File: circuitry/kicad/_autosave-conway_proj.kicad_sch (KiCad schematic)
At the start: 5 parts, among them J1 Power, J2 Digital/PWM, J3 Analog, J4 Digital/PWM

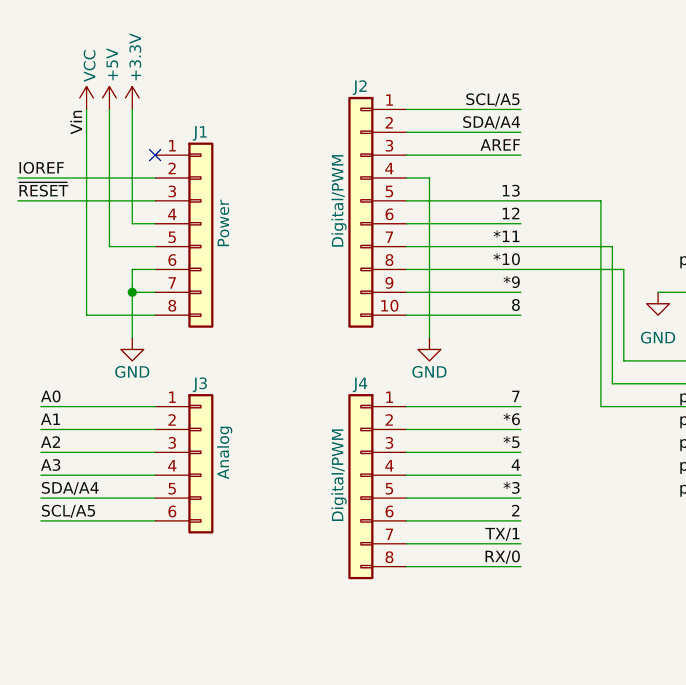
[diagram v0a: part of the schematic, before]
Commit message: New KiCad version and README updates
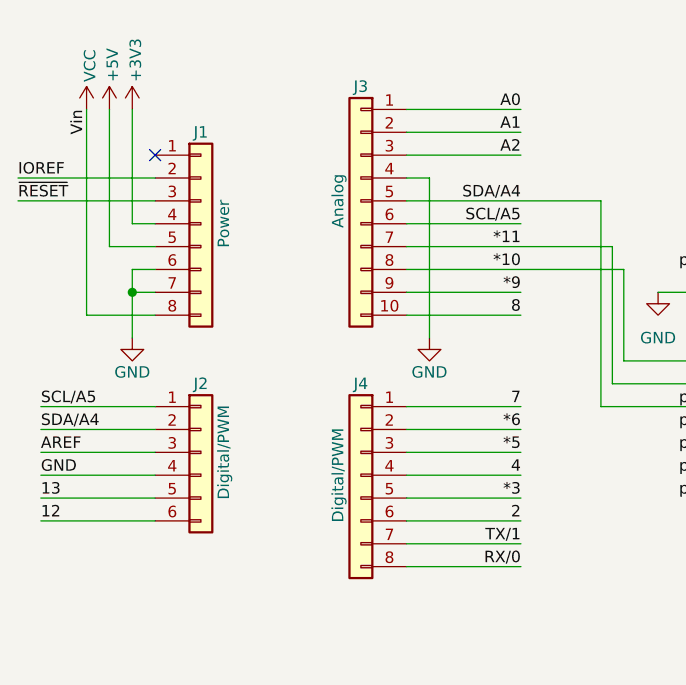
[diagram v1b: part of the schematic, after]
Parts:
- J2: renamed from J3; value Analog -> Digital/PWM; footprint Connector_PinSocket_2.54mm:PinSocket_1x06_P2.54mm_Vertical -> Connector_PinSocket_2.54mm:PinSocket_1x10_P2.54mm_Vertical
- J3: renamed from J2; value Digital/PWM -> Analog; footprint Connector_PinSocket_2.54mm:PinSocket_1x10_P2.54mm_Vertical -> Connector_PinSocket_2.54mm:PinSocket_1x06_P2.54mm_Vertical
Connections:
- net A3 is gone; now on net GND: J2.4 (Pin_4)
- net 12: now also J2.6 (Pin_6); no longer J3.6 (Pin_6)
- net 13: now also J2.5 (Pin_5); no longer DS1.6 (DB2), J3.5 (Pin_5)
- net A0: now also J3.1 (Pin_1); no longer J2.1 (Pin_1)
- net A1: now also J3.2 (Pin_2); no longer J2.2 (Pin_2)
- net A2: now also J3.3 (Pin_3); no longer J2.3 (Pin_3)
- net AREF: now also J2.3 (Pin_3); no longer J3.3 (Pin_3)
- net SCL/A5: now also J2.1 (Pin_1), J3.6 (Pin_6); no longer J2.6 (Pin_6), J3.1 (Pin_1)
- net SDA/A4: now also DS1.6 (DB2), J2.2 (Pin_2), J3.5 (Pin_5); no longer J2.5 (Pin_5), J3.2 (Pin_2)
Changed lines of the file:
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@@
     (effects (font (size 1.27 1.27)) (justify right bottom))
   )
-  (label "A2" (at 21.59 64.77 0) (fields_autoplaced)
+  (label "AREF" (at 21.59 64.77 0) (fields_autoplaced)
     (effects (font (size 1.27 1.27)) (justify left bottom))
   )
@@
     (effects (font (size 1.27 1.27)) (justify right bottom))
   )
-  (label "A3" (at 21.59 67.31 0) (fields_autoplaced)
+  (label "GND" (at 21.59 67.31 0) (fields_autoplaced)
     (effects (font (size 1.27 1.27)) (justify left bottom))
   )
@@
     (effects (font (size 1.27 1.27)) (justify right bottom))
   )
-  (label "13" (at 74.93 36.83 180) (fields_autoplaced)
-    (effects (font (size 1.27 1.27)) (justify right bottom))
-  )
-  (label "12" (at 74.93 39.37 180) (fields_autoplaced)
+  (label "SDA{slash}A4" (at 74.93 36.83 180) (fields_autoplaced)
+    (effects (font (size 1.27 1.27)) (justify right bottom))
+  )
+  (label "SCL{slash}A5" (at 74.93 39.37 180) (fields_autoplaced)
     (effects (font (size 1.27 1.27)) (justify right bottom))
   )
@@
     (effects (font (size 1.27 1.27)) (justify right bottom))
   )
-  (label "SDA{slash}A4" (at 74.93 29.21 180) (fields_autoplaced)
+  (label "A1" (at 74.93 29.21 180) (fields_autoplaced)
     (effects (font (size 1.27 1.27)) (justify right bottom))
   )
@@
     (effects (font (size 1.27 1.27)) (justify right bottom))
   )
-  (label "A1" (at 21.59 62.23 0) (fields_autoplaced)
+  (label "SDA{slash}A4" (at 21.59 62.23 0) (fields_autoplaced)
     (effects (font (size 1.27 1.27)) (justify left bottom))
   )
@@
     (effects (font (size 1.27 1.27)) (justify right bottom))
   )
-  (label "A0" (at 21.59 59.69 0) (fields_autoplaced)
-    (effects (font (size 1.27 1.27)) (justify left bottom))
-  )
-  (label "AREF" (at 74.93 31.75 180) (fields_autoplaced)
+  (label "SCL{slash}A5" (at 21.59 59.69 0) (fields_autoplaced)
+    (effects (font (size 1.27 1.27)) (justify left bottom))
+  )
+  (label "A2" (at 74.93 31.75 180) (fields_autoplaced)
     (effects (font (size 1.27 1.27)) (justify right bottom))
   )
@@
     (effects (font (size 1.27 1.27)) (justify right bottom))
   )
-  (label "SCL{slash}A5" (at 74.93 26.67 180) (fields_autoplaced)
+  (label "A0" (at 74.93 26.67 180) (fields_autoplaced)
     (effects (font (size 1.27 1.27)) (justify right bottom))
   )
@@
     (effects (font (size 1.27 1.27)) (justify left bottom))
   )
-  (label "SDA{slash}A4" (at 21.59 69.85 0) (fields_autoplaced)
-    (effects (font (size 1.27 1.27)) (justify left bottom))
-  )
-  (label "SCL{slash}A5" (at 21.59 72.39 0) (fields_autoplaced)
+  (label "13" (at 21.59 69.85 0) (fields_autoplaced)
+    (effects (font (size 1.27 1.27)) (justify left bottom))
+  )
+  (label "12" (at 21.59 72.39 0) (fields_autoplaced)
     (effects (font (size 1.27 1.27)) (justify left bottom))
   )
@@
   (symbol (lib_id "power:+3V3") (at 31.75 26.67 0) (unit 1)
     (in_bom yes) (on_board yes) (dnp no)
-    (property "Reference" "#PWR03" (at 31.75 30.48 0)
-      (effects (font (size 1.27 1.27)) hide)
-    )
-    (property "Value" "+3.3V" (at 32.131 23.622 90)
+    (property "Reference" "#PWR0106" (at 31.75 30.48 0)
+      (effects (font (size 1.27 1.27)) hide)
+    )
+    (property "Value" "+3V3" (at 32.131 23.622 90)
       (effects (font (size 1.27 1.27)) (justify left))
     )
@@
       (project "conway_proj"
         (path "/e63e39d7-6ac0-4ffd-8aa3-1841a4541b55"
-          (reference "#PWR03") (unit 1)
+          (reference "#PWR0106") (unit 1)
         )
       )
@@
   (symbol (lib_id "power:+5V") (at 29.21 26.67 0) (unit 1)
     (in_bom yes) (on_board yes) (dnp no)
-    (property "Reference" "#PWR02" (at 29.21 30.48 0)
+    (property "Reference" "#PWR0104" (at 29.21 30.48 0)
       (effects (font (size 1.27 1.27)) hide)
     )
@@
       (project "conway_proj"
         (path "/e63e39d7-6ac0-4ffd-8aa3-1841a4541b55"
-          (reference "#PWR02") (unit 1)
+          (reference "#PWR0104") (unit 1)
         )
       )
@@
   (symbol (lib_id "power:GND") (at 31.75 52.07 0) (unit 1)
     (in_bom yes) (on_board yes) (dnp no)
-    (property "Reference" "#PWR04" (at 31.75 58.42 0)
+    (property "Reference" "#PWR0103" (at 31.75 58.42 0)
       (effects (font (size 1.27 1.27)) hide)
     )
@@
       (project "conway_proj"
         (path "/e63e39d7-6ac0-4ffd-8aa3-1841a4541b55"
-          (reference "#PWR04") (unit 1)
+          (reference "#PWR0103") (unit 1)
         )
       )
@@
   (symbol (lib_id "Connector_Generic:Conn_01x10") (at 57.15 36.83 0) (mirror y) (unit 1)
     (in_bom yes) (on_board yes) (dnp no)
-    (property "Reference" "J2" (at 57.15 24.13 0)
-      (effects (font (size 1.27 1.27)))
-    )
-    (property "Value" "Digital/PWM" (at 54.61 36.83 90)
-      (effects (font (size 1.27 1.27)))
-    )
-    (property "Footprint" "Connector_PinSocket_2.54mm:PinSocket_1x10_P2.54mm_Vertical" (at 57.15 36.83 0)
+    (property "Reference" "J3" (at 57.15 24.13 0)
+      (effects (font (size 1.27 1.27)))
+    )
+    (property "Value" "Analog" (at 54.61 36.83 90)
+      (effects (font (size 1.27 1.27)))
+    )
+    (property "Footprint" "Connector_PinSocket_2.54mm:PinSocket_1x06_P2.54mm_Vertical" (at 57.15 36.83 0)
       (effects (font (size 1.27 1.27)) hide)
     )
@@
       (project "conway_proj"
         (path "/e63e39d7-6ac0-4ffd-8aa3-1841a4541b55"
-          (reference "J2") (unit 1)
+          (reference "J3") (unit 1)
         )
       )
@@
   (symbol (lib_id "power:GND") (at 64.77 52.07 0) (unit 1)
     (in_bom yes) (on_board yes) (dnp no)
-    (property "Reference" "#PWR05" (at 64.77 58.42 0)
+    (property "Reference" "#PWR0107" (at 64.77 58.42 0)
       (effects (font (size 1.27 1.27)) hide)
     )
@@
       (project "conway_proj"
         (path "/e63e39d7-6ac0-4ffd-8aa3-1841a4541b55"
-          (reference "#PWR05") (unit 1)
+          (reference "#PWR0107") (unit 1)
         )
       )
@@
   (symbol (lib_id "Connector_Generic:Conn_01x06") (at 39.37 64.77 0) (unit 1)
     (in_bom yes) (on_board yes) (dnp no)
-    (property "Reference" "J3" (at 39.37 57.15 0)
-      (effects (font (size 1.27 1.27)))
-    )
-    (property "Value" "Analog" (at 41.91 64.77 90)
-      (effects (font (size 1.27 1.27)))
-    )
-    (property "Footprint" "Connector_PinSocket_2.54mm:PinSocket_1x06_P2.54mm_Vertical" (at 39.37 64.77 0)
+    (property "Reference" "J2" (at 39.37 57.15 0)
+      (effects (font (size 1.27 1.27)))
+    )
+    (property "Value" "Digital/PWM" (at 41.91 64.77 90)
+      (effects (font (size 1.27 1.27)))
+    )
+    (property "Footprint" "Connector_PinSocket_2.54mm:PinSocket_1x10_P2.54mm_Vertical" (at 39.37 64.77 0)
       (effects (font (size 1.27 1.27)) hide)
     )
@@
       (project "conway_proj"
         (path "/e63e39d7-6ac0-4ffd-8aa3-1841a4541b55"
-          (reference "J3") (unit 1)
+          (reference "J2") (unit 1)
         )
       )
@@
   (symbol (lib_id "power:GND") (at 106.68 30.48 0) (unit 1)
     (in_bom yes) (on_board yes) (dnp no) (fields_autoplaced)
-    (property "Reference" "#PWR07" (at 106.68 36.83 0)
+    (property "Reference" "#PWR0101" (at 106.68 36.83 0)
       (effects (font (size 1.27 1.27)) hide)
     )
@@
       (project "conway_proj"
         (path "/e63e39d7-6ac0-4ffd-8aa3-1841a4541b55"
-          (reference "#PWR07") (unit 1)
+          (reference "#PWR0101") (unit 1)
         )
       )
@@
   (symbol (lib_id "power:+5V") (at 130.81 54.61 0) (unit 1)
     (in_bom yes) (on_board yes) (dnp no) (fields_autoplaced)
-    (property "Reference" "#PWR08" (at 130.81 58.42 0)
+    (property "Reference" "#PWR0110" (at 130.81 58.42 0)
       (effects (font (size 1.27 1.27)) hide)
     )
@@
       (project "conway_proj"
         (path "/e63e39d7-6ac0-4ffd-8aa3-1841a4541b55"
-          (reference "#PWR08") (unit 1)
+          (reference "#PWR0110") (unit 1)
         )
       )
@@
   (symbol (lib_id "power:VCC") (at 26.67 26.67 0) (unit 1)
     (in_bom yes) (on_board yes) (dnp no)
-    (property "Reference" "#PWR01" (at 26.67 30.48 0)
+    (property "Reference" "#PWR0105" (at 26.67 30.48 0)
       (effects (font (size 1.27 1.27)) hide)
     )
@@
       (project "conway_proj"
         (path "/e63e39d7-6ac0-4ffd-8aa3-1841a4541b55"
-          (reference "#PWR01") (unit 1)
+          (reference "#PWR0105") (unit 1)
         )
       )
@@
   (symbol (lib_id "power:GND") (at 130.81 59.69 0) (unit 1)
     (in_bom yes) (on_board yes) (dnp no) (fields_autoplaced)
-    (property "Reference" "#PWR09" (at 130.81 66.04 0)
+    (property "Reference" "#PWR0109" (at 130.81 66.04 0)
       (effects (font (size 1.27 1.27)) hide)
     )
@@
       (project "conway_proj"
         (path "/e63e39d7-6ac0-4ffd-8aa3-1841a4541b55"
-          (reference "#PWR09") (unit 1)
+          (reference "#PWR0109") (unit 1)
         )
       )
@@
   (symbol (lib_id "power:GND") (at 90.17 46.99 0) (unit 1)
     (in_bom yes) (on_board yes) (dnp no) (fields_autoplaced)
-    (property "Reference" "#PWR010" (at 90.17 53.34 0)
+    (property "Reference" "#PWR0102" (at 90.17 53.34 0)
       (effects (font (size 1.27 1.27)) hide)
     )
@@
       (project "conway_proj"
         (path "/e63e39d7-6ac0-4ffd-8aa3-1841a4541b55"
-          (reference "#PWR010") (unit 1)
+          (reference "#PWR0102") (unit 1)
         )
       )
@@
   (symbol (lib_id "power:+5V") (at 106.68 78.74 0) (unit 1)
     (in_bom yes) (on_board yes) (dnp no) (fields_autoplaced)
-    (property "Reference" "#PWR06" (at 106.68 82.55 0)
+    (property "Reference" "#PWR0108" (at 106.68 82.55 0)
       (effects (font (size 1.27 1.27)) hide)
     )
@@
       (project "conway_proj"
         (path "/e63e39d7-6ac0-4ffd-8aa3-1841a4541b55"
-          (reference "#PWR06") (unit 1)
-        )
-      )
+          (reference "#PWR0108") (unit 1)
+        )
+      )
